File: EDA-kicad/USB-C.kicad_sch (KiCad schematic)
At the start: 5 parts, among them J5 USBC-3-2-fix-USB4056-03-A_REV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

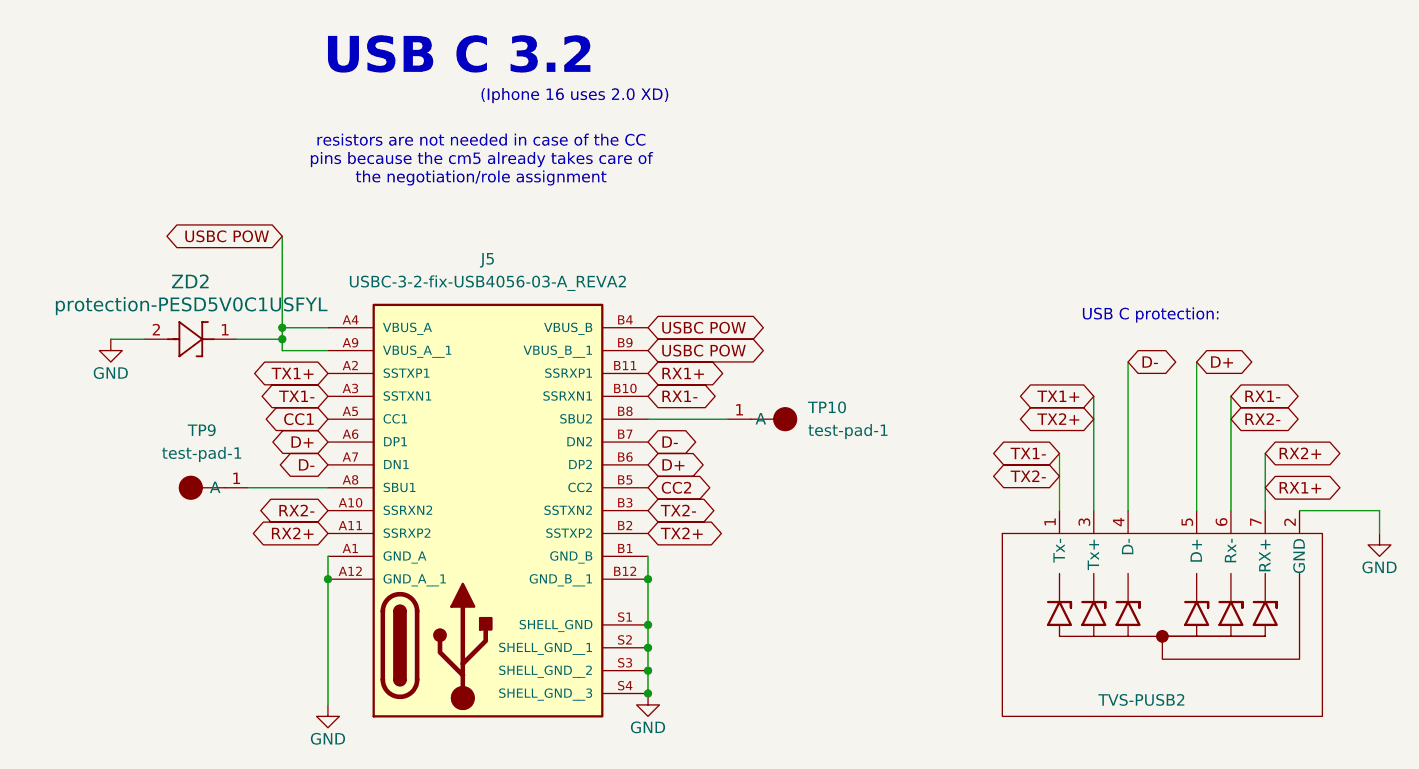
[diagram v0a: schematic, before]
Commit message: schematic cleaned up a bit
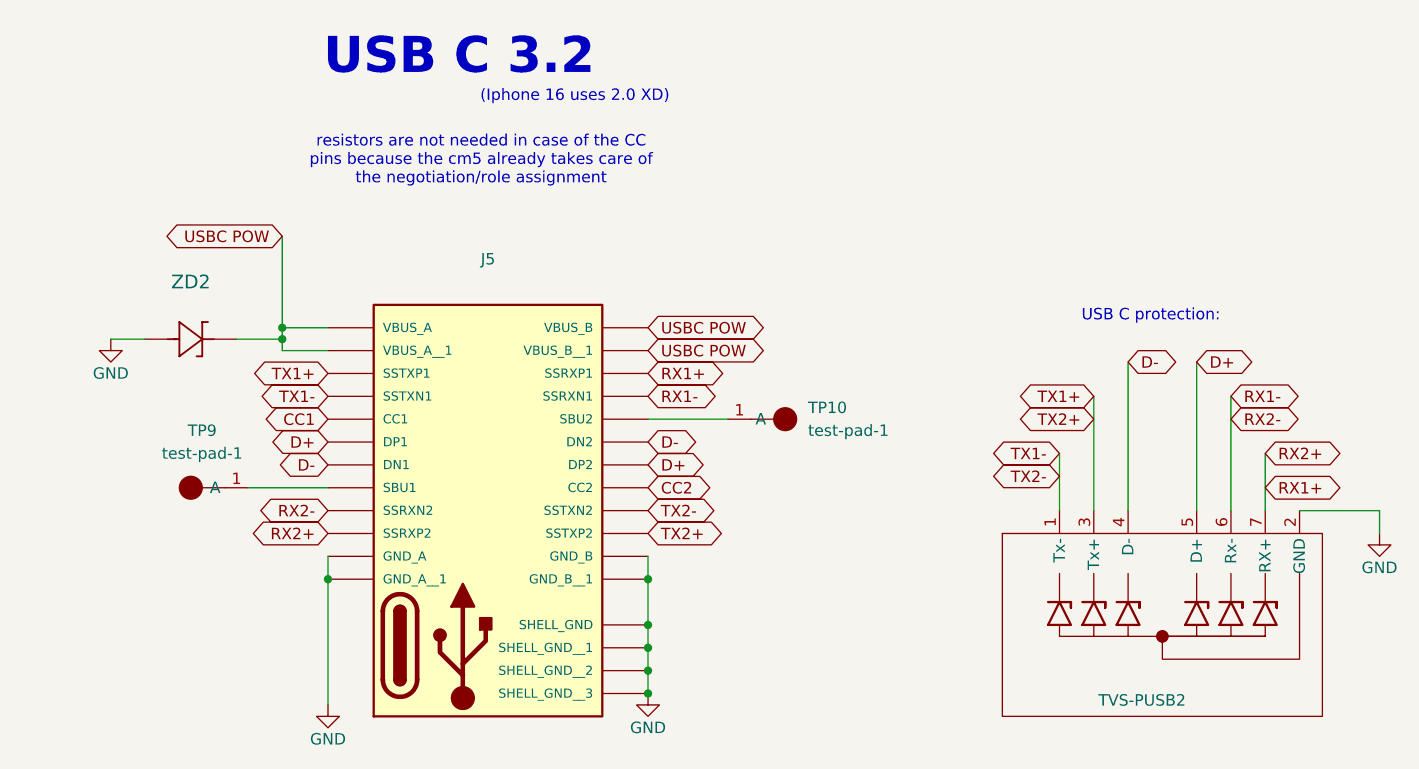
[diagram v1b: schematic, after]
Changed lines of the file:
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@@
 					(size 1.524 1.524)
 				)
+				(hide yes)
 			)
 		)
@@
 					(size 1.27 1.27)
 				)
+				(hide yes)
 			)
 		)

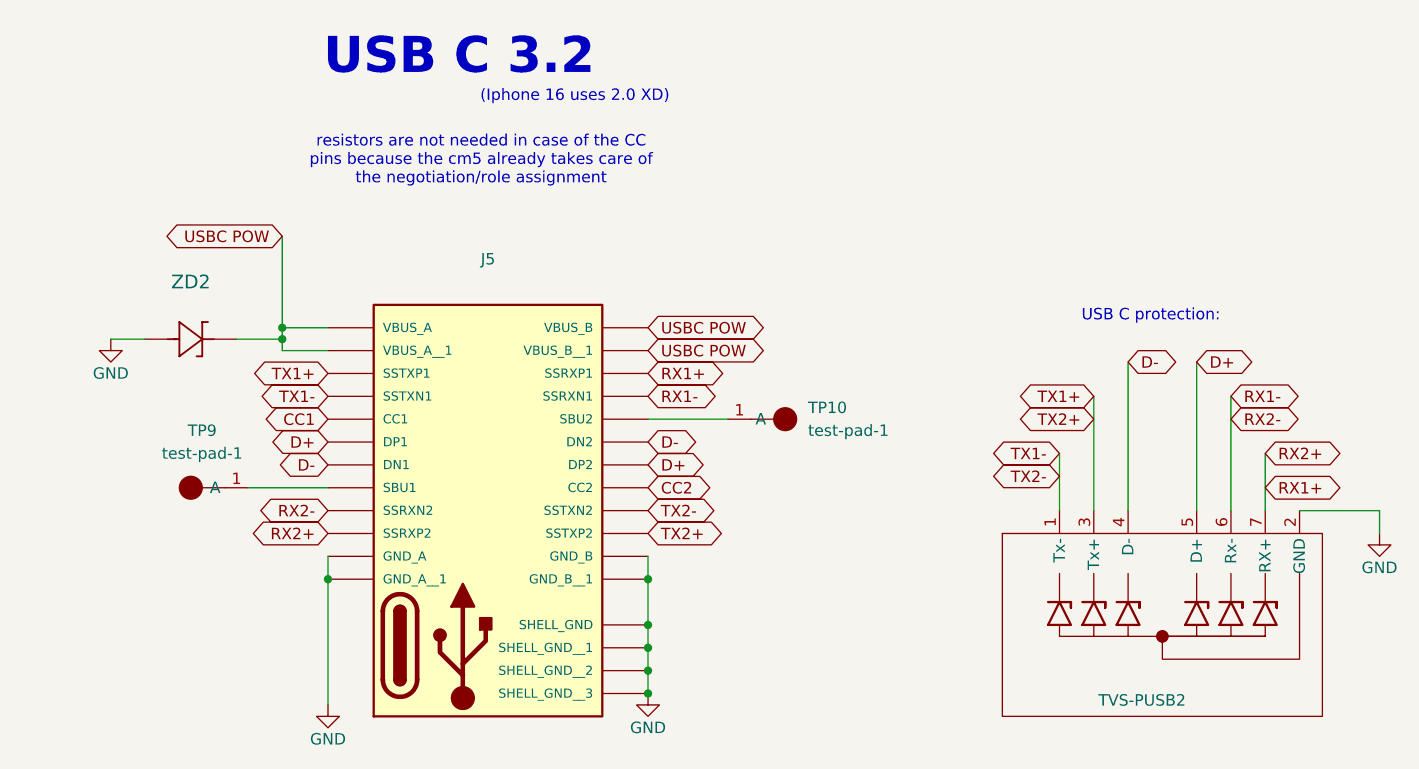
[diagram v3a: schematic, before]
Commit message: remove SBU test pads from USB C
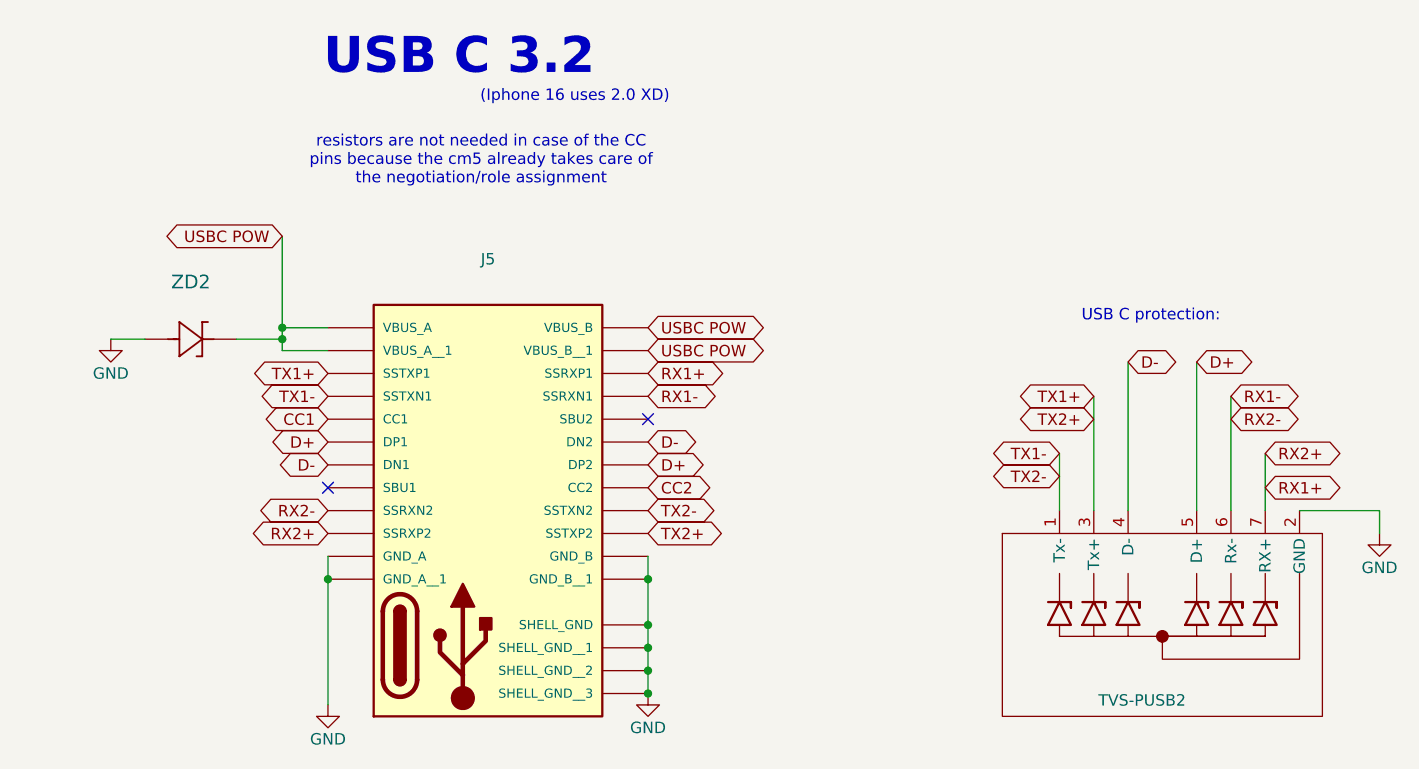
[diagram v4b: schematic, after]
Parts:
- removed TP10, TP9: test-pad-1, SPIRIT-footprints:test-pad-1, symbol SPIRIT-components:test-pad-1
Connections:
- no-connect marks 0 -> 2
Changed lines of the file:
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@@
 		(color 0 0 0 0)
 	)
+	(no_connect
+		(at 97.79 107.95)
+	)
+	(no_connect
+		(at 133.35 100.33)
+	)
 	(wire
 		(pts
@@
 	(wire
 		(pts
-			(xy 133.35 100.33) (xy 142.24 100.33)
-		)
-		(stroke
-			(width 0)
-			(type default)
-		)
-	)
-	(wire
-		(pts
 			(xy 92.71 92.71) (xy 92.71 91.44)
 		)
@@
 	(wire
 		(pts
-			(xy 88.9 107.95) (xy 97.79 107.95)
-		)
-		(stroke
-			(width 0)
-			(type default)
-		)
-	)
-	(wire
-		(pts
 			(xy 77.47 91.44) (xy 73.66 91.44)
 		)
@@
 			"pcB5nuvAZmYWQEdWvcCVRvTAZmYWQPGevMC95ezAZmYWQIqYu8B5ytbAZmYWQGxhqcChAgAAAAAA"
 			"AKD8RYEOVgAAwBz/46V/AAAsAAAAIAAAADIAAAAwAAAAOAAAACAAAABwAAAAaQAAAG4AAAAgAAAA"
-			"KAAAAGgAAAB0AAAAdAAAAHAAAAA6AAAALwAAAC8AAAB3AAAAdw=="
+			"KAAAAGgAAAB0AAAAdAAAAHAAAAA6AAAALwAAAC8AAAB3AAAAdwAAAFgAAABiAAAAdAAAADIAAAA3"
+			"AAAAYgAAADcAAAA4AAAAOAAAAGsAAAB0AAAARgAAAFYAAABoAAAAZwAAAHcAAAAzAAAALwAAAGYA"
+			"AABGAAAAdwAAADQAAAA2AAAAUQAAAEMAAABQAAAARwAAAC8AAABBAAAAQwAAADYAAAB6AAAAWAAA"
+			"AHkAAAB1AAAAWQAAAG4AAABSAAAARAAAAG0AAAB1AAAAdQAAADcAAABZAAAAcwAAAFcAAABNAAAA"
+			"bgAAAFQAAAA1AAAANgAAAE0AAABTAAAAUwAAAHIAAABwAAAAZAAAAEYAAAByAAAAVAAAAHQAAABF"
+			"AAAAegAAAEcAAAB3AAAAbAAAAHEAAABqAAAAegAAAFoAAABzAAAAMwAAAHYAAAArAAAASwAAAEsA"
+			"AABLAAAAMAAAADQAAAArAAAAKwAAAFcAAABRAAAATQAAAG4AAABqAAAANQAAAFMAAABiAAAARAAA"
+			"AFIAAABoAAAAMQAAAEsAAABkAAAAdQAAACsAAAB4AAAANgAAAG4AAABDAAAAMQAAADUAAABzAAAA"
+			"LwAAAFYAAABmAAAAegAAAHEAAABFAAAAMAAAAFUAAABRAAAAYgAAAGYAAAA4AAAAcQAAAHAAAABC"
+			"AAAAbAAAAEQAAABCAAAASAAAAGkAAAB0AAAAdwAAAGQAAABqAAAAYgAAAE8AAABuAAAAUwAAAHAA"
+			"AABiAAAATgAAAG4AAAB6AAAAOQAAADYAAAAwAAAAYQAAAFoAAABPAAAAcQAAAHEAAABwAAAAUgAA"
+			"AFMAAAB3AAAAegAAAEEAAABJAAAASQAAAGEAAABKAAAASQAAAHMAAABiAAAAegAAAHcAAABWAAAA"
+			"VgAAAGQAAABkAAAAOQAAAGMAAABBAAAARAAAAEQAAAArAAAARAAAAHEAAABDAAAAUQAAAEMAAAB1"
+			"AAAANgAAADMAAABQAAAANQAAAGIAAABsAAAARQAAAFUAAABmAAAAMQAAAHkAAABtAAAAQQAAAHcA"
+			"AABDAAAAMgAAAGIAAAA5AAAAOAAAACsAAABkAAAAKwAAADcAAABjAAAAbgAAAGoAAAAxAAAANwAA"
+			"AG4AAABuAAAAcgAAAHEAAABxAAAAUgAAAEIAAABZAAAAQgAAAHcAAAArAAAAYwAAAFQAAAA4AAAA"
+			"SQAAADAAAAB6AAAARQAAAE8AAABBAAAAbQAAAHgAAABRAAAAWQAAAGcAAAB1AAAARAAAADcAAABm"
+			"AAAAagAAAEsAAABaAAAALwAAAFAAAABqAAAAagAAAGoAAAArAAAAUAAAAHgAAAB1AAAASwAAAHoA"
+			"AABJAAAAYwAAACsAAABiAAAATwAAADAAAABWAAAAVAAAAE4AAABgcmKuKX8AAMCdYq4pfwAAULBi"
+			"ril/AAAQn2KuKX8AAOCqYq4pfwAAAIViril/AAAwjGKuKX8AAJCCYq4pfwAAYI1iril/AADQg2Ku"
+			"KX8AAPCKYq4pfwAAYFVyril/AAAwBGWuKX8AAPAFZa4pfwAAUARlril/AAAgBmWuKX8AAHAEZa4p"
+			"fwAAQAZlril/AACgBGWuKX8AAHAGZa4pfwAA0ARlril/AACgBmWuKX8AAPAEZa4pfwAA0AZlril/"
+			"AAAABWWuKX8AAPAGZa4pfwAAMAVlril/AAAgB2WuKX8AAEAiZa4pfwAAQGpgril/AAAQdmCuKX8A"
+			"AOB9YK4pfwAAYGtgril/AAAwCG+uKX8AAPAiZa4pfwAAwGtgril/AABwB2+uKX8AAMCPYK4pfwAA"
+			"sJRgril/AAAggmCuKX8AANAVb64pfwAAEBZvril/AADAFW+uKX8AAHBsYK4pfwAAcAlvril/AAAQ"
+			"pGCuKX8AADCOYK4pfwAAwAlwril/AACwv2+uKX8AAHCIZK4pfwAA4Alwril/AABQC3CuKX8AAHAK"
+			"cK4pfwAAsAxwril/AABQDXCuKX8AAFAOcK4pfwAAEGxyril/AADQJWWuKX8AAHBocq4pfwAAENxv"
+			"ril/AAAArHGuKX8AAJAOcK4pfwAA0Mlvril/AABAEnCuKX8AAAAScK4pfwAAABNwril/AADAE3Cu"
+			"KX8AACAScK4pfwAAYAtyril/AADgCHKuKX8AAEAJcq4pfwAAMHFyril/AABgbnKuKX8AANBtcq4p"
+			"fwAAcG9yril/AADQFHCuKX8AAAAVcK4pfwAAUEZwril/AABQGnCuKX8AAKDjZK4pfwAA0OVkril/"
+			"AACA5mSuKX8AAHAwZa4pfwAAUDRlril/AAAAQmWuKX8AAJBFZa4pfwAAIDFlril/AACANWWuKX8A"
+			"ALBCZa4pfwAAwEZlril/AAAQMmWuKX8AALA2Za4pfwAAgENlril/AADwR2WuKX8AACAzZa4pfwAA"
+			"4Ddlril/AABwRGWuKX8AACBJZa4pfwAAoFJlril/AADgU2WuKX8AACBVZa4pfwAAwC9lril/AADQ"
+			"HHCuKX8AAHD6Ya4pfwAAAPhhril/AADw8GGuKX8AAIDuYa4pfwAAwOthril/AADw6GGuKX8AAEDg"
+			"Ya4pfwAAMN1hril/AADg2WGuKX8AALDWYa4pfwAAoM1hril/AABgymGuKX8AAMDGYa4pfwAAEMNh"
+			"ril/AABwv2GuKX8AACC8Ya4pfwAA0Lhhril/AAAwtWGuKX8AANCxYa4pfwAAoK5hril/AAAAq2Gu"
+			"KX8AACCoYa4pfwAAwJ5hril/AADwmmGuKX8AAMCXYa4pfwAAkA=="
 		)
 	)
@@
 	)
 	(symbol
-		(lib_id "SPIRIT-components:test-pad-1")
-		(at 148.59 99.06 0)
-		(unit 1)
-		(exclude_from_sim no)
-		(in_bom yes)
-		(on_board yes)
-		(dnp no)
-		(fields_autoplaced yes)
-		(property "Reference" "TP10"
-			(at 151.13 99.0599 0)
-			(effects
-				(font
-					(size 1.27 1.27)
-				)
-				(justify left)
-			)
-		)
-		(property "Value" "test-pad-1"
-			(at 151.13 101.5999 0)
-			(effects
-				(font
-					(size 1.27 1.27)
-				)
-				(justify left)
-			)
-		)
-		(property "Footprint" "SPIRIT-footprints:test-pad-1"
-			(at 148.59 99.06 0)
-			(effects
-				(font
-					(size 1.27 1.27)
-				)
-				(hide yes)
-			)
-		)
-		(property "Datasheet" ""
-			(at 148.59 99.06 0)
-			(effects
-				(font
-					(size 1.27 1.27)
-				)
-				(hide yes)
-			)
-		)
-		(property "Description" ""
-			(at 148.59 99.06 0)
-			(effects
-				(font
-					(size 1.27 1.27)
-				)
-				(hide yes)
-			)
-		)
-		(pin "1"
-		)
-		(instances
-			(project "cm5-carrier"
-				(path "/28c5e4fe-1ec7-4477-97f0-d2ec1401fad5/4d20c3c8-7f3b-4711-a43f-15c2a08af985"
-					(reference "TP10")
-					(unit 1)
-				)
-			)
-		)
-	)
-	(symbol
 		(lib_id "power:GND")
 		(at 133.35 130.81 0)
@@
 					(unit 1)
 				)
-			)
-		)
-	)
-	(symbol
-		(lib_id "SPIRIT-components:test-pad-1")
-		(at 82.55 109.22 180)
-		(unit 1)
-		(exclude_from_sim no)
-		(in_bom yes)
-		(on_board yes)
-		(dnp no)
-		(fields_autoplaced yes)
-		(property "Reference" "TP9"
-			(at 83.82 101.6 0)
-			(effects
-				(font
-					(size 1.27 1.27)
-				)
-			)
-		)
-		(property "Value" "test-pad-1"
-			(at 83.82 104.14 0)
-			(effects
-				(font
-					(size 1.27 1.27)
-				)
-			)
-		)
-		(property "Footprint" "SPIRIT-footprints:test-pad-1"
-			(at 82.55 109.22 0)
-			(effects
-				(font
-					(size 1.27 1.27)
-				)
-				(hide yes)
-			)
-		)
-		(property "Datasheet" ""
-			(at 82.55 109.22 0)
-			(effects
-				(font
-					(size 1.27 1.27)
-				)
-				(hide yes)
-			)
-		)
-		(property "Description" ""
-			(at 82.55 109.22 0)
-			(effects
-				(font
-					(size 1.27 1.27)
-				)
-				(hide yes)
-			)
-		)
-		(pin "1"
-		)
-		(instances
-			(project "cm5-carrier"
-				(path "/28c5e4fe-1ec7-4477-97f0-d2ec1401fad5/4d20c3c8-7f3b-4711-a43f-15c2a08af985"
-					(reference "TP9")
-					(unit 1)
-				)

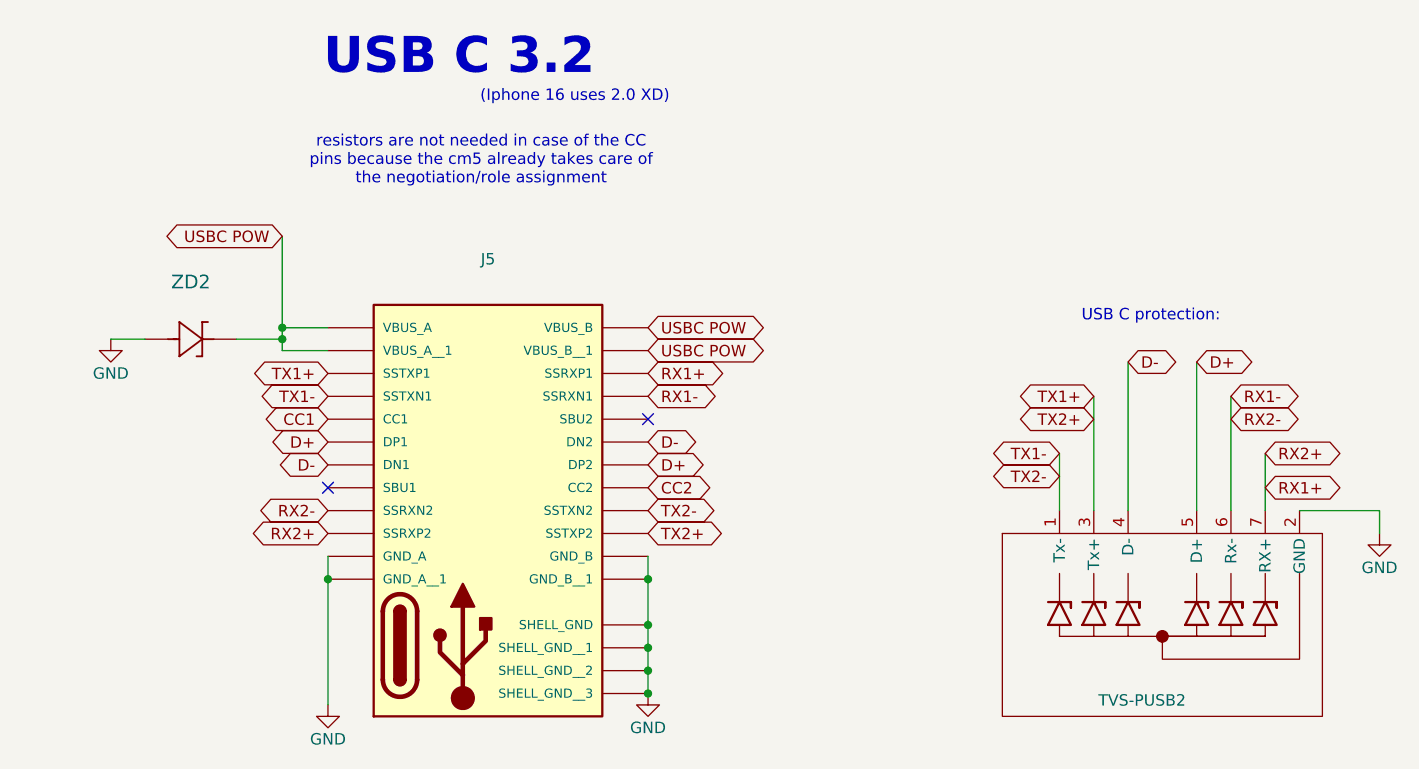
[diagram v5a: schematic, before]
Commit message: upgrade usb c to waterproof and 4-0
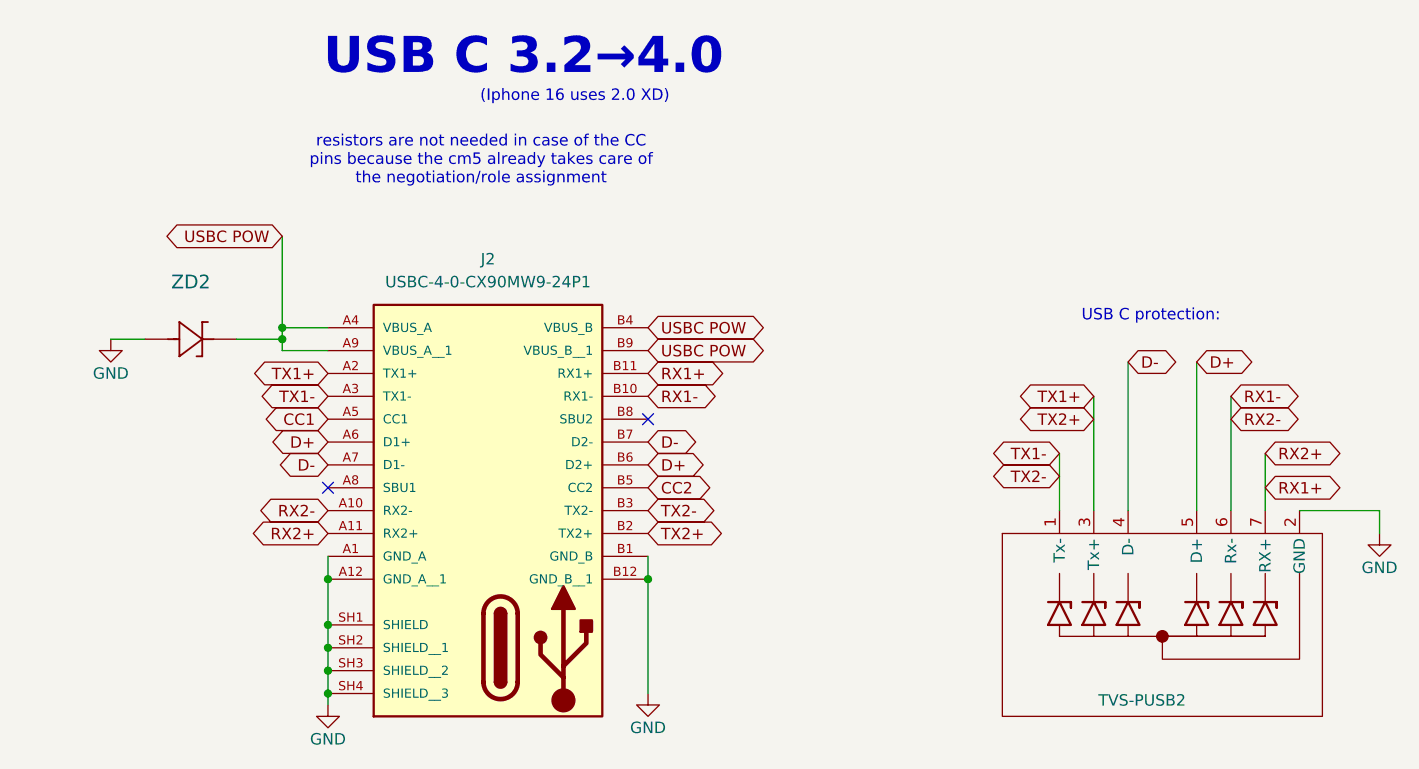
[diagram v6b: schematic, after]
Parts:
- removed J5: USBC-3-2-fix-USB4056-03-A_REVA2, SPIRIT-footprints:USBC-3-2-fix-GCT_USB4056-03-A_REVA2, symbol SPIRIT-components:USBC-3-2-fix-USB4056-03-A_REVA2
- added J2: USBC-4-0-CX90MW9-24P1, SPIRIT-footprints:USB-4-0-HIROSE_CX90MW9-24P1, symbol SPIRIT-components:USBC-4-0-CX90MW9-24P1
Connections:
- net CC1: now also J2.A5 (CC1)
- net CC2: now also J2.B5 (CC2)
- net D+: now also J2.A6 (D1+), J2.B6 (D2+)
- net D-: now also J2.A7 (D1-), J2.B7 (D2-)
- net GND: now also J2.A1 (GND_A), J2.A12 (GND_A__1), J2.B1 (GND_B), J2.B12 (GND_B__1), J2.SH1 (SHIELD), J2.SH2 (SHIELD__1), J2.SH3 (SHIELD__2), J2.SH4 (SHIELD__3)
- net RX1+: now also J2.A11 (RX2+), J2.B11 (RX1+)
- net RX1-: now also J2.A10 (RX2-), J2.B10 (RX1-)
- net TX1+: now also J2.A2 (TX1+), J2.B2 (TX2+)
- net TX1-: now also J2.A3 (TX1-), J2.B3 (TX2-)
- net USBC POW: now also J2.A4 (VBUS_A), J2.A9 (VBUS_A__1), J2.B4 (VBUS_B), J2.B9 (VBUS_B__1)
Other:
- note added: "USB C 3.2→4.0"
- note removed: "USB C 3.2"
